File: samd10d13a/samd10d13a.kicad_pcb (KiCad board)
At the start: 2 copper layers, 17 parts, among them J1 USB_C_Receptacle_PWR_Only, J2 Conn_01x10_Male, J3 Conn_01x07_Male, J4 Conn_ARM_JTAG_SWD_10, SW1 SW_SPST, U1 NJM2866F, U2 ATSAMD10D13A-SS

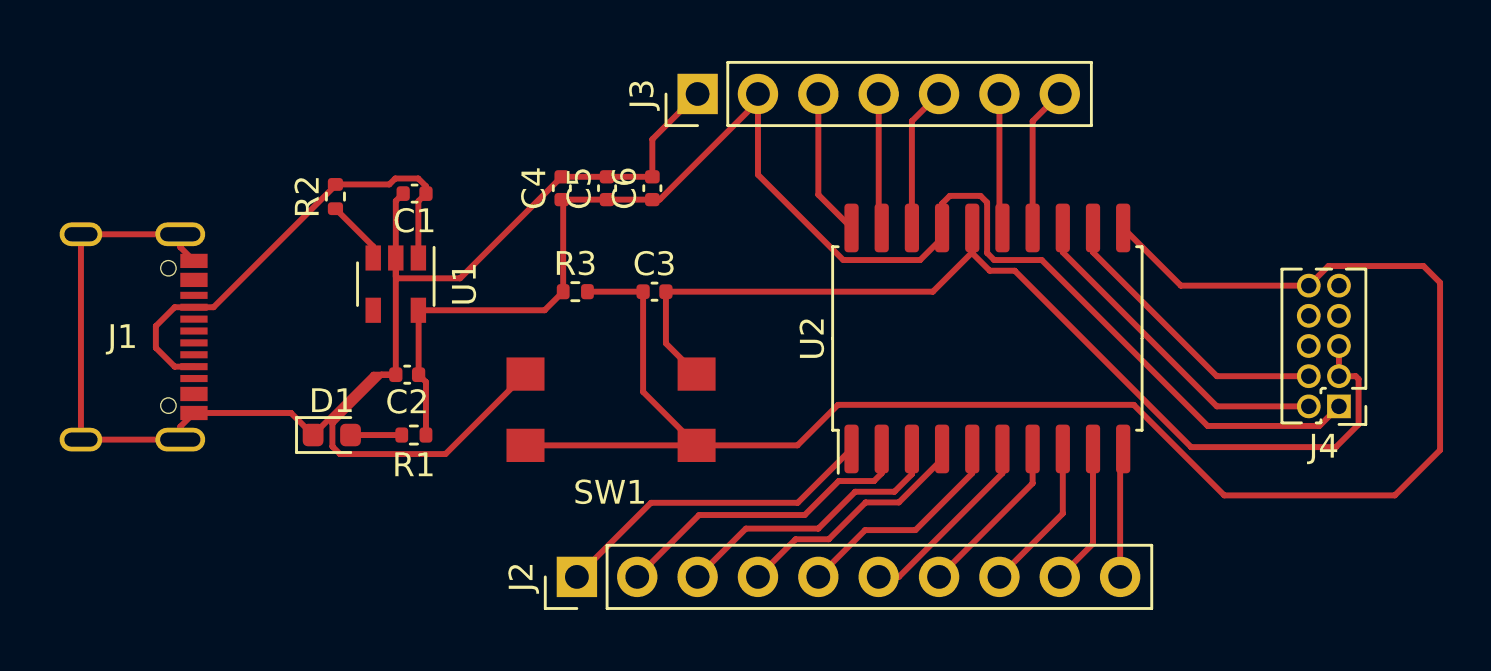
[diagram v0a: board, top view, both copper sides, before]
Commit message: finished samd10 pipsqueek v0 (ordered)
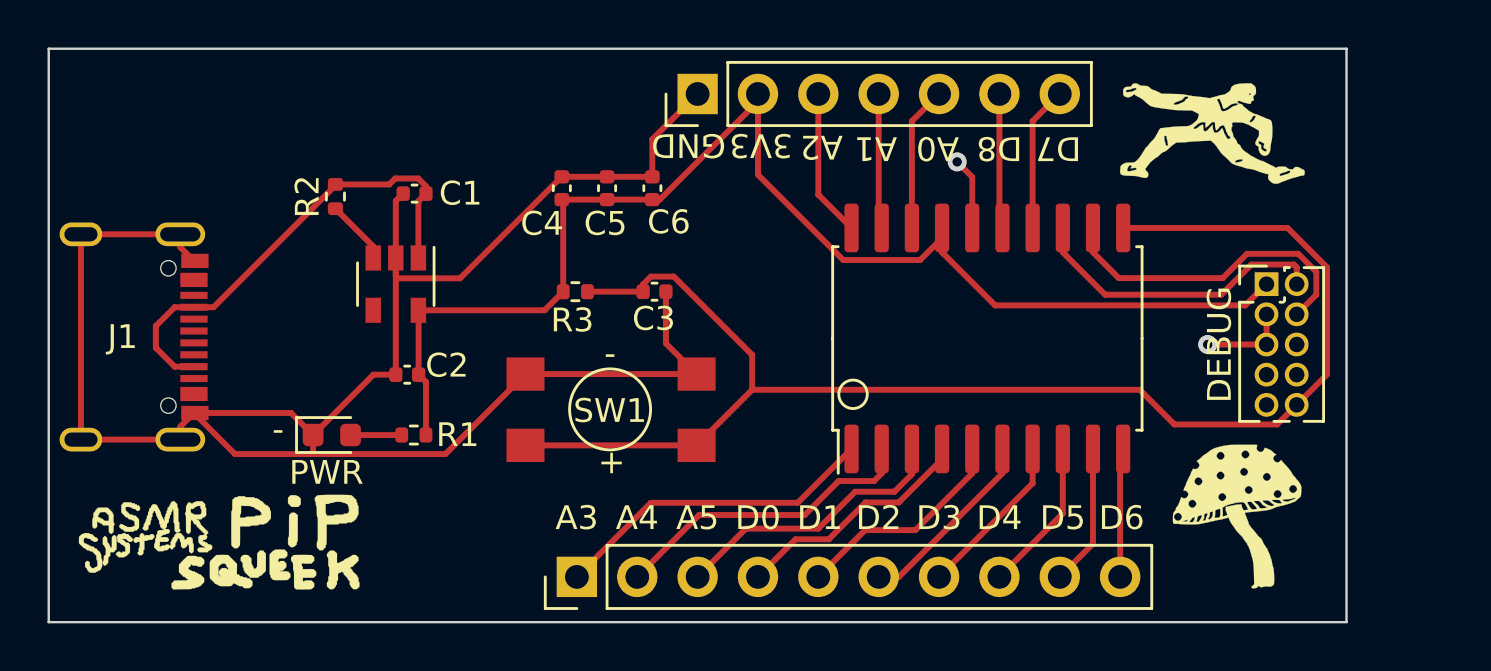
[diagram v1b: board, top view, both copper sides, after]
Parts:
- added G***: LOGO, ASMR_footprints:SilkScreen_Champion, F.Cu at (122.9, 50.0)
- added G***: LOGO, ASMR_footprints:SilkScreen_Mushroom, F.Cu at (124.5, 65.9)
- added G***: LOGO, ASMR_footprints:Logo_samd10_pipsqueek, F.Cu at (81.5, 67.1)
- moved J4 5.98 mm to (125.5, 56.3), turned to 0 degrees
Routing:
- net GND: track 112.9 -> 89.9 mm, vias 0 -> 2
- net RST: track 73.3 -> 60.2 mm
- net +3V3: track 62.9 -> 55.4 mm
- net SWCLK: track 12.3 -> 13.7 mm
- net SWDIO: track 14.1 -> 12.9 mm
- added copper zone on B.Cu, net GND
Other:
- board outline added: 54.6 x 24.1 mm
- board text added: "+"
- board text added: "-"
- board text added: "3V3"
- board text added: "A0"
- board text added: "A1"
- board text added: "A2"
- board text added: "A3"
- board text added: "A4"
- board text added: "A5"
- board text added: "D0"
- board text added: "D1"
- board text added: "D2"
- board text added: "D3"
- board text added: "D4"
- board text added: "D5"
- board text added: "D6"
- board text added: "D7"
- board text added: "D8"
- board text added: "DEBUG"
- board text added: "GND"
- board text added: "PWR"

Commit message: fix samd10 pipsqueek dev board, update footprint for usbc receptacle/power reg symbol name, generate gerbers/drill files
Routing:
- net VDD: track 20.1 -> 22.3 mm

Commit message: finished samd21 dev board (syzygy), exported gerbers and drill files
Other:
- board text added: "v2"
